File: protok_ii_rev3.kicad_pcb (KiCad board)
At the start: 2 copper layers, 199 parts, among them J1 Conn_01x04_Male, J2 Conn_01x04_Male, SW1 Rotary_Encoder, U1 proton_c, U2 MCP23017_SO

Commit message: update schematic
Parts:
- added J3: Conn_01x02_Male, Connector_PinHeader_2.54mm:PinHeader_1x02_P2.54mm_Horizontal, F.Cu at (-11.7, 100.9)
- added J4: Conn_01x09_Male, Connector_PinHeader_2.54mm:PinHeader_1x09_P2.54mm_Horizontal, F.Cu at (-25.1, 100.9)
- added R7: 10K, Resistor_SMD:R_0402_1005Metric, F.Cu at (-26.0, 124.5)
- added R8: 10K, Resistor_SMD:R_0402_1005Metric, F.Cu at (-12.6, 115.0)
- added S1: 1825910-6, digikey-footprints:Switch_Tactile_THT_6x6mm, F.Cu at (-12.1, 107.6)
- added S2: 1825910-6, digikey-footprints:Switch_Tactile_THT_6x6mm, F.Cu at (1.25, 100.4)
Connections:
- U1 pad A0: Net-(U1-PadA0) -> A0
- U1 pad A1: Net-(U1-PadA1) -> A1
- U1 pad A10: Net-(U1-PadA10) -> RX
- U1 pad A13: Net-(U1-PadA13) -> Row6
- U1 pad A14: Net-(U1-PadA14) -> Row5
- U1 pad A15: Net-(U1-PadA15) -> Row1
- U1 pad A2: Net-(U1-PadA2) -> A2
- U1 pad A6: Net-(U1-PadA6) -> Y1
- U1 pad A7: Net-(U1-PadA7) -> X1
- U1 pad A8: Net-(U1-PadA8) -> Row0
- U1 pad A9: Net-(U1-PadA9) -> TX
- U1 pad B0: Net-(U1-PadB0) -> A1
- U1 pad B1: Net-(U1-PadB1) -> B1
- U1 pad B10: Net-(U1-PadB10) -> Row2
- U1 pad B11: Net-(U1-PadB11) -> Row3
- U1 pad B12: Net-(U1-PadB12) -> Row4
- U1 pad B13: Net-(U1-PadB13) -> SCLK
- U1 pad B14: Net-(U1-PadB14) -> MISO
- U1 pad B15: Net-(U1-PadB15) -> MOSI
- U1 pad B2: Net-(U1-PadB2) -> A2
- U1 pad B3: Net-(U1-PadB3) -> B2
- U1 pad B4: Net-(U1-PadB4) -> A3
- U1 pad B5: Net-(U1-PadB5) -> B3
- U1 pad B6: Net-(U1-PadB6) -> SCL
- U1 pad B7: Net-(U1-PadB7) -> SDA
- U1 pad B8: Net-(U1-PadB8) -> B8
- U1 pad B9: Net-(U1-PadB9) -> J_EN
- U1 pad DFU: Net-(U1-PadDFU) -> DFU
- U1 pad GND: Net-(U1-PadGND) -> GND
- U1 pad RST: Net-(U1-PadRST) -> RST

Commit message: finish pcb
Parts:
- removed the J3 at (-11.7, 100.9)
- removed the R4 at (55.2, 92.3)
- removed the R5 at (52.3, 92.3)
- removed R7, R8: 10K, Resistor_SMD:R_0402_1005Metric
- removed S1, S2: 1825910-6, digikey-footprints:Switch_Tactile_THT_6x6mm
- added BZ1: Buzzer, my_lib:AST1109MLTRQ, F.Cu at (114.3, 47.3)
- added J1: AudioPlug4, my_lib:3.5mm_phone_jack_THT, F.Cu at (164.4, 33.9)
- added P1: USB_C_Plug, my_lib:TYPE-C-31-M-04, B.Cu at (177.4, 31.0)
- added R3: 5.1K, Resistor_SMD:R_0402_1005Metric, B.Cu at (171.3, 36.3)
- added REF**: MountingHole_2.2mm_M2, MountingHole:MountingHole_2.2mm_M2, F.Cu at (346.6, 80.7)
- added REF**: MountingHole_2.2mm_M2, MountingHole:MountingHole_2.2mm_M2, F.Cu at (346.6, 175.9)
- added REF**: MountingHole_2.2mm_M2, MountingHole:MountingHole_2.2mm_M2, F.Cu at (268.0, 175.9)
- added REF**: MountingHole_2.2mm_M2, MountingHole:MountingHole_2.2mm_M2, F.Cu at (163.3, 161.9)
- added REF**: MountingHole_2.2mm_M2, MountingHole:MountingHole_2.2mm_M2, F.Cu at (99.0, 161.9)
- added REF**: MountingHole_2.2mm_M2, MountingHole:MountingHole_2.2mm_M2, F.Cu at (232.3, 80.7)
- added REF**: MountingHole_2.2mm_M2, MountingHole:MountingHole_2.2mm_M2, F.Cu at (137.1, 66.7)
- added REF**: MountingHole_2.2mm_M2, MountingHole:MountingHole_2.2mm_M2, F.Cu at (75.2, 85.7)
- added REF**: MountingHole_2.2mm_M2, MountingHole:MountingHole_2.2mm_M2, F.Cu at (89.7, 118.8)
- added REF**: MountingHole_2.2mm_M2, MountingHole:MountingHole_2.2mm_M2, F.Cu at (208.8, 118.8)
- added REF**: MountingHole_2.5mm, MountingHole:MountingHole_2.5mm, F.Cu at (165.6, 118.8)
- added REF**: MountingHole_2.5mm, MountingHole:MountingHole_2.5mm, F.Cu at (241.8, 118.8)
- added REF**: MountingHole_2.2mm_M2, MountingHole:MountingHole_2.2mm_M2, F.Cu at (346.9, 118.8)
- C1, R1, R2, U2: moved to B.Cu
- D1: renamed from D93; moved to B.Cu
- D10: renamed from D9; moved to B.Cu
- D11: renamed from D10; moved to B.Cu
- D12: renamed from D11; moved to B.Cu
- D13: renamed from D12; moved to B.Cu
- D14: renamed from D13; moved to B.Cu
- D15: renamed from D14; moved to B.Cu
- D16: renamed from D15; moved to B.Cu
- D17: renamed from D16; moved to B.Cu
- D18: renamed from D17; moved to B.Cu
- D19: renamed from D18; moved to B.Cu
- D2: renamed from D1; moved to B.Cu
- D20: renamed from D19; moved to B.Cu
- D21: renamed from D20; moved to B.Cu
- D22: renamed from D21; moved to B.Cu
- D23: renamed from D22; moved to B.Cu
- D24: renamed from D23; moved to B.Cu
- D25: renamed from D24; moved to B.Cu
- D26: renamed from D25; moved to B.Cu
- D27: renamed from D26; moved to B.Cu
- D28: renamed from D27; moved to B.Cu
- D29: renamed from D28; moved to B.Cu
- D3: renamed from D2; moved to B.Cu
- D30: renamed from D29; moved to B.Cu
- D31: renamed from D30; moved to B.Cu
- D32: renamed from D31; moved to B.Cu
- D33: renamed from D32; moved to B.Cu
- D34: renamed from D33; moved to B.Cu
- D35: renamed from D34; moved to B.Cu
- D36: renamed from D35; moved to B.Cu
- D37: renamed from D36; moved to B.Cu
- D38: renamed from D37; moved to B.Cu
- D39: renamed from D38; moved to B.Cu
- D4: renamed from D3; moved to B.Cu
- D40: renamed from D39; moved to B.Cu
- D41: renamed from D40; moved to B.Cu
- D42: renamed from D41; moved to B.Cu
- D43: renamed from D42; moved to B.Cu
- D44: renamed from D43; moved to B.Cu
- D45: renamed from D44; moved to B.Cu
- D46: renamed from D45; moved to B.Cu
- D47: renamed from D46; moved to B.Cu
- D48: renamed from D47; moved to B.Cu
- D49: renamed from D48; moved to B.Cu
- D5: renamed from D4; moved to B.Cu
- D50: renamed from D49; moved to B.Cu
- D51: renamed from D50; moved to B.Cu
- D52: renamed from D51; moved to B.Cu
- D53: renamed from D52; moved to B.Cu
- D54: renamed from D53; moved to B.Cu
- D55: renamed from D54; moved to B.Cu
- D56: renamed from D55; moved to B.Cu
- D57: renamed from D56; moved to B.Cu
- D58: renamed from D57; moved to B.Cu
- D59: renamed from D58; moved to B.Cu
- D6: renamed from D5; moved to B.Cu
- D60: renamed from D59; moved to B.Cu
- D61: renamed from D60; moved to B.Cu
- D62: renamed from D61; moved to B.Cu
- D63: renamed from D62; moved to B.Cu
- D64: renamed from D63; moved to B.Cu
- D65: renamed from D64; moved to B.Cu
- D66: renamed from D65; moved to B.Cu
- D67: renamed from D66; moved to B.Cu
- D68: renamed from D67; moved to B.Cu
- D69: renamed from D68; moved to B.Cu
- D7: renamed from D6; moved to B.Cu
- D70: renamed from D69; moved to B.Cu
- D71: renamed from D70; moved to B.Cu
- D72: renamed from D71; moved to B.Cu
- D73: renamed from D72; moved to B.Cu
- D74: renamed from D73; moved to B.Cu
- D75: renamed from D74; moved to B.Cu
- D76: renamed from D75; moved to B.Cu
- D77: renamed from D76; moved to B.Cu
- D78: renamed from D77; moved to B.Cu
- D79: renamed from D78; moved to B.Cu
- D8: renamed from D7; moved to B.Cu
- D80: renamed from D79; moved to B.Cu
- D81: renamed from D80; moved to B.Cu
- D82: renamed from D81; moved to B.Cu
- D83: renamed from D82; moved to B.Cu
- D84: renamed from D83; moved to B.Cu
- D85: renamed from D84; moved to B.Cu
- D86: renamed from D85; moved to B.Cu
- D87: renamed from D86; moved to B.Cu
- D88: renamed from D87; moved to B.Cu
- D89: renamed from D88; moved to B.Cu
- D9: renamed from D8; moved to B.Cu
- D90: renamed from D89; moved to B.Cu
- D91: renamed from D90; moved to B.Cu
- D92: renamed from D91; moved to B.Cu
- D93: renamed from D92; moved to B.Cu
- J2: value Conn_01x04_Male -> Conn_01x10_Male; footprint my_lib:MKI2C-2V -> Connector_PinHeader_2.54mm:PinHeader_1x10_P2.54mm_Horizontal
- J3: renamed from J1; moved to B.Cu
- J4: value Conn_01x09_Male -> Conn_01x04_Male; footprint Connector_PinHeader_2.54mm:PinHeader_1x09_P2.54mm_Horizontal -> Connector_PinHeader_2.54mm:PinHeader_1x04_P2.54mm_Horizontal
- R4: renamed from R3; moved to B.Cu
- R5: renamed from R6; moved to B.Cu
- moved D90 313.3 mm to (355.6, 158.5), turned to 270 degrees
- moved D93 310.6 mm to (352.9, 175.9), turned to 270 degrees
- moved K_DEL1 309.6 mm to (351.3, 109.3)
- moved D89 295.8 mm to (343.4, 158.5), turned to 270 degrees
- moved D92 294.2 mm to (341.4, 175.9), turned to 270 degrees
- moved END1 292.7 mm to (356.1, 90.2)
- moved D91 275.4 mm to (327.3, 175.9), turned to 270 degrees
- moved K_RIGHT1 272.6 mm to (356.1, 185.5)
- moved J4 271.2 mm to (238.4, 36.6), turned to 270 degrees
- moved D88 270.6 mm to (323.1, 158.5), turned to 270 degrees
- moved D75 265.1 mm to (351.3, 153.8), turned to 90 degrees
- moved D74 264.2 mm to (323.7, 152.9), turned to 90 degrees
- moved K_LEFT1 254.7 mm to (318.0, 185.5)
- moved D61 251.9 mm to (351.3, 134.7), turned to 90 degrees
- moved J2 247.6 mm to (223.4, 36.6), turned to 270 degrees
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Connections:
- J2 pad 1: GND -> +3V3
- J2 pad 2: SDA -> GND
- J2 pad 3: SCL -> SA2
- J2 pad 4: +3V3 -> SA1
- J4 pad 1: +3V3 -> GND
- J4 pad 2: GND -> +3V3
- J4 pad 3: A2 -> SCL
- J4 pad 4: A1 -> SDA
- R4 pad 1: Net-(R3-Pad1) -> Net-(R4-Pad1)
- R5 pad 1: Net-(R6-Pad1) -> Net-(R5-Pad1)
- U1 pad 5V: Net-(U1-Pad5V) -> VBUS
- U1 pad A1: A1 -> SA1
- U1 pad A2: A2 -> SA2
- U1 pad A4: Net-(U1-PadA4) -> SPK
- U1 pad A5: Net-(U1-PadA5) -> J_EN
- U1 pad B0: A1 -> A3
- U1 pad B1: B1 -> B3
- U1 pad B2: A2 -> A1
- U1 pad B3: B2 -> B1
- U1 pad B4: A3 -> A2
- U1 pad B5: B3 -> B2
- U1 pad B9: J_EN -> B9
- U1 pad D+: Net-(U1-PadD+) -> D+
- U1 pad D-: Net-(U1-PadD-) -> D-
- U1 pad DFU: DFU -> Net-(U1-PadDFU)
- U1 pad RST: RST -> Net-(U1-PadRST)
- U2 pad 15: Net-(R6-Pad1) -> Net-(R5-Pad1)
- U2 pad 17: Net-(R4-Pad1) -> Net-(R5-Pad1)
- U2 pad 18: Net-(R3-Pad1) -> Net-(R4-Pad1)
- U2 pad 19: Net-(R7-Pad1) -> Net-(R4-Pad1)
- U2 pad 20: Net-(R8-Pad1) -> Net-(R4-Pad1)
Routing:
- net Row1: track 0.00 -> 474.9 mm
- net Row4: track 0.00 -> 405.7 mm, vias 0 -> 1
- net Row5: track 0.00 -> 400.9 mm, vias 0 -> 1
- net Col0: track 0.00 -> 390.3 mm
- net Row3: track 0.00 -> 376.8 mm, vias 0 -> 1
- net Row6: track 0.00 -> 369.2 mm, vias 0 -> 1
- net Row2: track 0.00 -> 355.4 mm, vias 0 -> 1
- net Col15: track 0.00 -> 327.6 mm
- net Col14: track 0.00 -> 313.4 mm
- net Col1: track 0.00 -> 312.8 mm
- net Row0: track 0.00 -> 299.4 mm
- net Col13: track 0.00 -> 278.1 mm
- net Col3: track 0.00 -> 258.4 mm
- net Col2: track 0.00 -> 254.2 mm
- net Col4: track 0.00 -> 238.1 mm
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- added copper zone on B.Cu, net GND
- added copper zone on F.Cu, net GND
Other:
- board outline added: 313.9 x 168.1 mm
- net class +3V3 added: clearance 0.2, trace_width 0.5, via_dia 0.8, via_drill 0.4

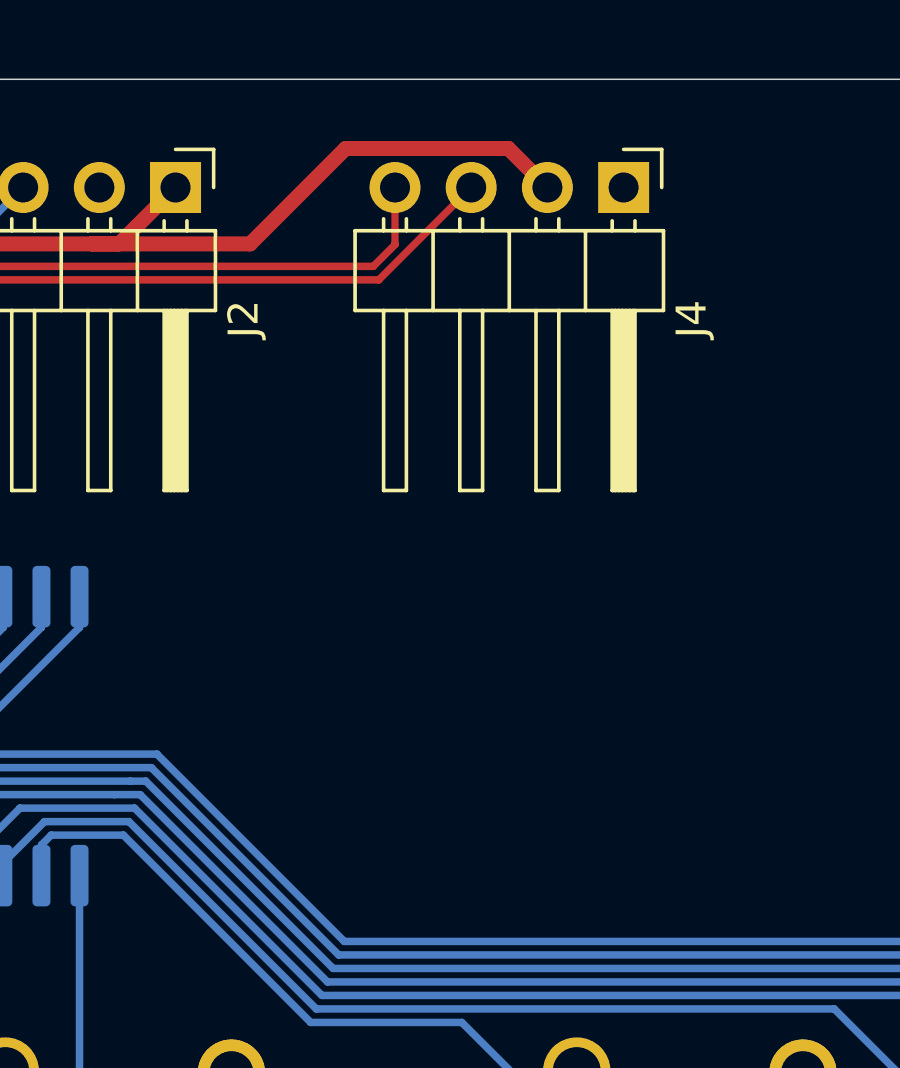
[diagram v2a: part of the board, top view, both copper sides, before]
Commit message: final version with eeprom
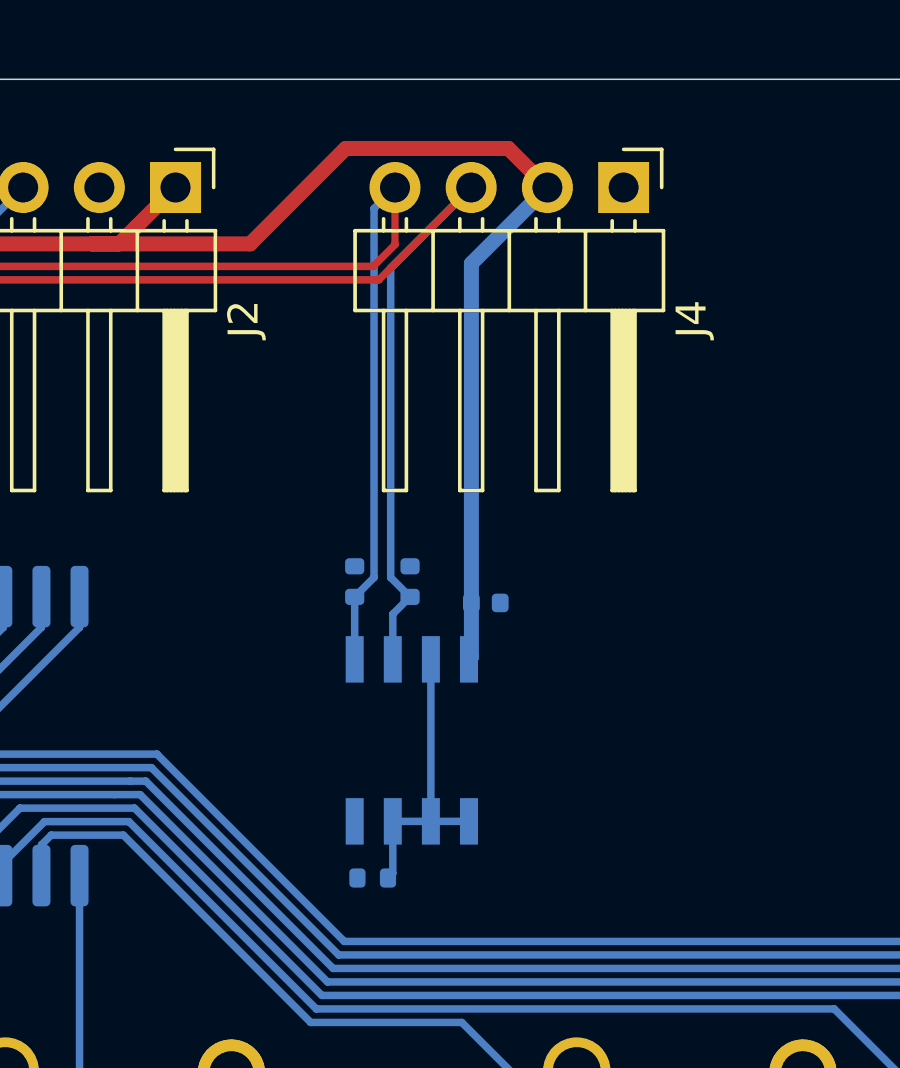
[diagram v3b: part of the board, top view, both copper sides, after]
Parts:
- added C2: 100nF, Capacitor_SMD:C_0402_1005Metric, B.Cu at (233.8, 50.4)
- added R6: 10K, Resistor_SMD:R_0402_1005Metric, B.Cu at (230.0, 59.6)
- added R7: 10K, Resistor_SMD:R_0402_1005Metric, B.Cu at (231.2, 49.7)
- added R8: 10K, Resistor_SMD:R_0402_1005Metric, B.Cu at (229.4, 49.7)
- added U3: AT24C256C-SSHL-B, my_lib:SOIC127P600X175-8N, B.Cu at (231.3, 55.0)
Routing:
- net SCL: track 142.7 -> 160.1 mm
- net +3V3: track 170.8 -> 187.6 mm
- net SDA: track 140.3 -> 156.6 mm
- net Net-(R6-Pad1): track 0.00 -> 9.89 mm

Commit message: add manufacturing file
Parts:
- added REF**: SMT_Tooling_Hole_JLCPCB, my_lib:SMT_Tooling_Hole_JLCPCB, F.Cu at (57.9, 174.1)
- added REF**: SMT_Tooling_Hole_JLCPCB, my_lib:SMT_Tooling_Hole_JLCPCB, F.Cu at (364.1, 193.5)
- added REF**: SMT_Tooling_Hole_JLCPCB, my_lib:SMT_Tooling_Hole_JLCPCB, F.Cu at (363.6, 35.7)
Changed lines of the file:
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@@
     (tracks 1606)
     (zones 0)
-    (modules 220)
+    (modules 223)
     (nets 166)
   )
@@
     (mod_text_size 1 1)
     (mod_text_width 0.15)
-    (pad_size 1.524 1.524)
-    (pad_drill 0.762)
+    (pad_size 1.3 1.3)
+    (pad_drill 1.152)
     (pad_to_mask_clearance 0)
     (aux_axis_origin 0 0)
@@
       (drillshape 0)
       (scaleselection 1)
-      (outputdirectory "./"))
+      (outputdirectory "/home/flyxian/project/protok_rev3_output/"))
   )
   (net 0 "")
@@
     (uvia_drill 0.1)
   )
+  (module my_lib:SMT_Tooling_Hole_JLCPCB (layer F.Cu)
+    (at 57.89325 174.057869)
+    (descr "Mounting Hole 2.1mm, no annular")
+    (tags "mounting hole 2.1mm no annular")
+    (attr virtual)
+    (fp_text reference REF** (at 0 -3.2) (layer Dwgs.User)
+      (effects (font (size 1 1) (thickness 0.15)))
+    )
+    (fp_text value SMT_Tooling_Hole_JLCPCB (at 0 3.2) (layer F.Fab)
+      (effects (font (size 1 1) (thickness 0.15)))
+    )
+    (fp_circle (center 0 0) (end 1.152 0) (layer Cmts.User) (width 0.15))
+    (fp_circle (center 0 0) (end 1.152 0) (layer F.CrtYd) (width 0.05))
+    (pad "" np_thru_hole circle (at 0 0) (size 1.3 1.3) (drill 1.152) (layers *.Cu *.Paste *.Mask)
+      (solder_mask_margin 0.124) (zone_connect 0))
+  )
+  (module my_lib:SMT_Tooling_Hole_JLCPCB (layer F.Cu)
+    (at 364.14105 193.526969)
+    (descr "Mounting Hole 2.1mm, no annular")
+    (tags "mounting hole 2.1mm no annular")
+    (attr virtual)
+    (fp_text reference REF** (at 0 -3.2) (layer Dwgs.User)
+      (effects (font (size 1 1) (thickness 0.15)))
+    )
+    (fp_text value SMT_Tooling_Hole_JLCPCB (at 0 3.2) (layer F.Fab)
+      (effects (font (size 1 1) (thickness 0.15)))
+    )
+    (fp_circle (center 0 0) (end 1.152 0) (layer Cmts.User) (width 0.15))
+    (fp_circle (center 0 0) (end 1.152 0) (layer F.CrtYd) (width 0.05))
+    (pad "" np_thru_hole circle (at 0 0) (size 1.3 1.3) (drill 1.152) (layers *.Cu *.Paste *.Mask)
+      (solder_mask_margin 0.124) (zone_connect 0))
+  )
+  (module my_lib:SMT_Tooling_Hole_JLCPCB (layer F.Cu)
+    (at 363.56955 35.691369)
+    (descr "Mounting Hole 2.1mm, no annular")
+    (tags "mounting hole 2.1mm no annular")
+    (attr virtual)
+    (fp_text reference REF** (at 0 -3.2) (layer Dwgs.User)
+      (effects (font (size 1 1) (thickness 0.15)))
+    )
+    (fp_text value SMT_Tooling_Hole_JLCPCB (at 0 3.2) (layer F.Fab)
+      (effects (font (size 1 1) (thickness 0.15)))
+    )
+    (fp_circle (center 0 0) (end 1.152 0) (layer Cmts.User) (width 0.15))
+    (fp_circle (center 0 0) (end 1.152 0) (layer F.CrtYd) (width 0.05))
+    (pad "" np_thru_hole circle (at 0 0) (size 1.3 1.3) (drill 1.152) (layers *.Cu *.Paste *.Mask)
+      (solder_mask_margin 0.124) (zone_connect 0))
+  )
   (module my_lib:SOIC127P600X175-8N (layer B.Cu)
